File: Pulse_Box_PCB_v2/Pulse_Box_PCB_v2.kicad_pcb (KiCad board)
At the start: 2 copper layers, 80 x 59 mm, 60 parts, among them J1 Screw_Terminal_01x02, J2 Conn_01x11, J3 Conn_01x11, J4 Conn_01x03, J5 Conn_01x03, J6 Conn_01x03_Pin, P1 USB_C_Plug_USB2.0, SW1 SW_Push, SW2 SW_Push, U1 ESP32-S3-WROOM-1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

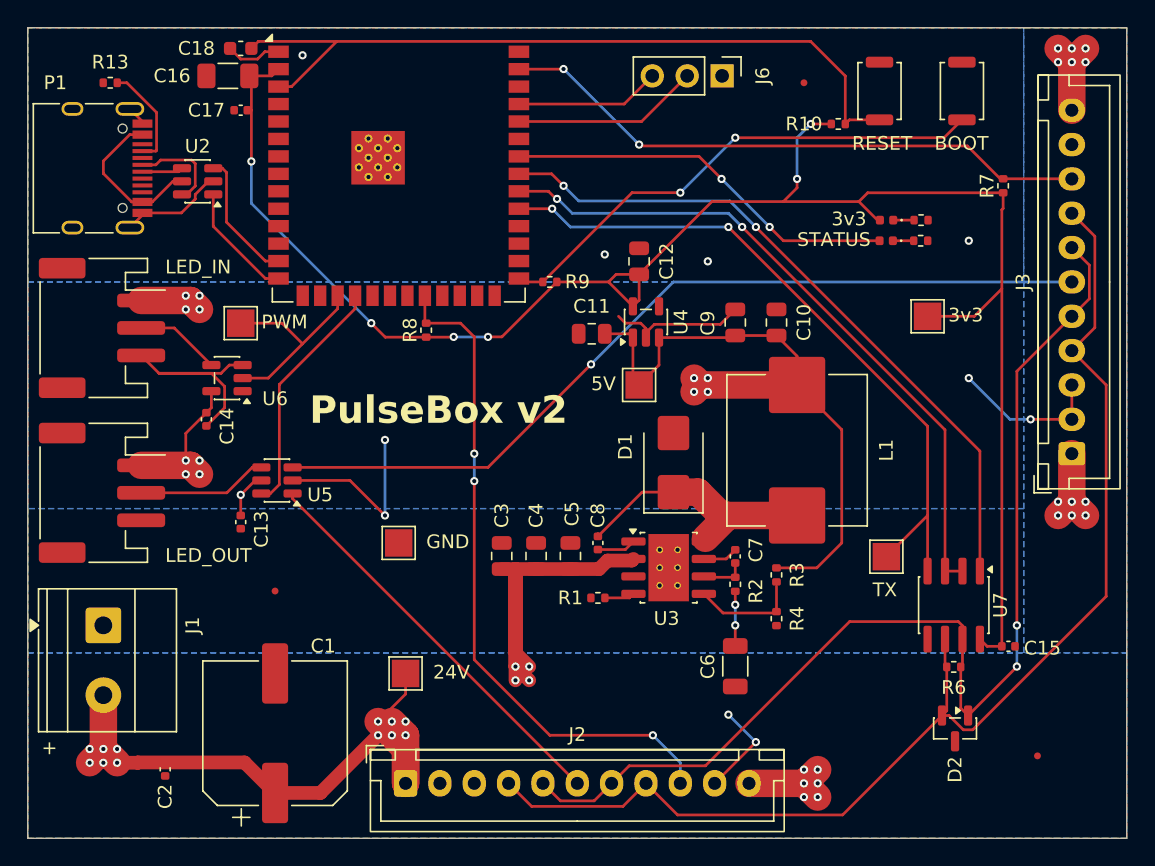
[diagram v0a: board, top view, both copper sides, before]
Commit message: add design for pulsebox panel, update v2 PCB to remove 485 trans
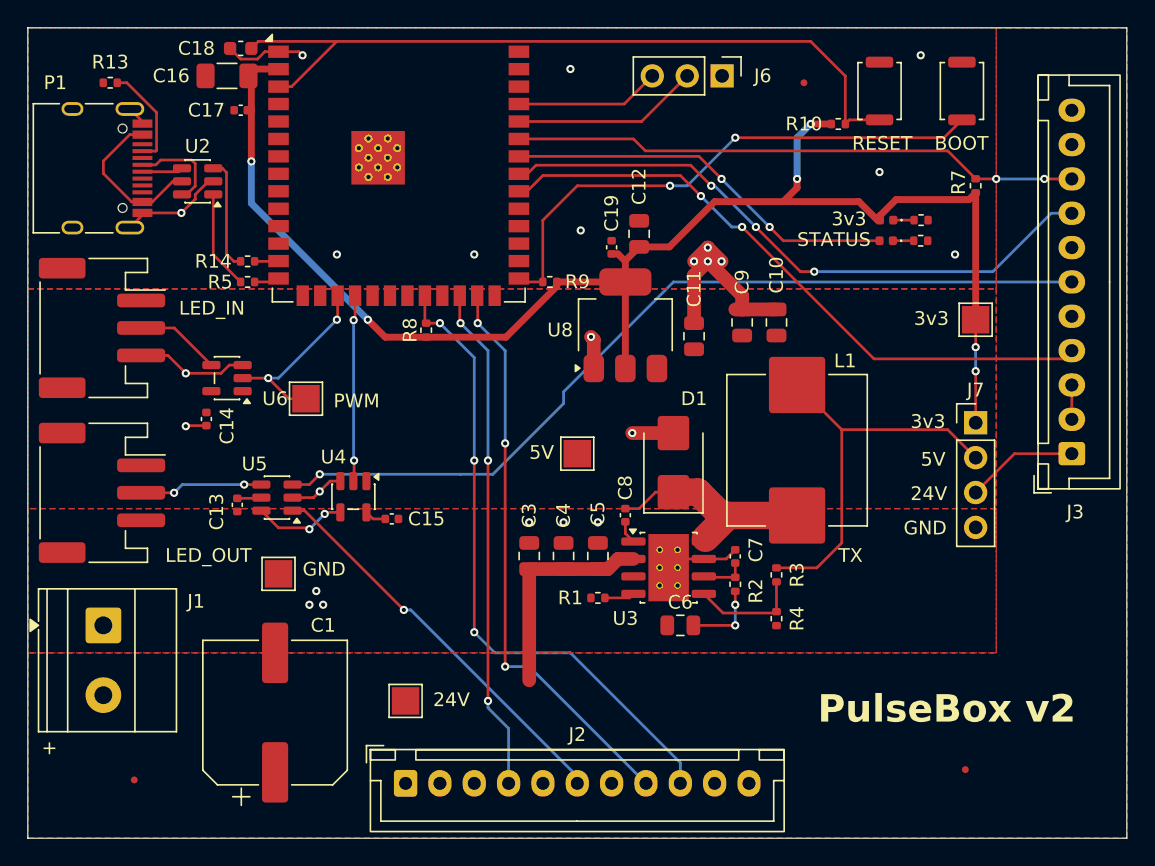
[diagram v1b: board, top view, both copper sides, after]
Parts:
- removed C2: 100nF, Capacitor_SMD:C_0402_1005Metric
- removed D2: SP0502BAHT, Package_TO_SOT_SMD:SOT-23
- removed R6: 120, Resistor_SMD:R_0402_1005Metric
- removed TP6: TestPoint, TestPoint:TestPoint_Pad_2.0x2.0mm
- removed U7: SP3485EN, Package_SO:SOIC-8_3.9x4.9mm_P1.27mm
- added C19: 100nF, Capacitor_SMD:C_0402_1005Metric, F.Cu at (192.5, 67.0)
- added J7: Conn_01x04, Connector_PinHeader_2.54mm:PinHeader_1x04_P2.54mm_Vertical, F.Cu at (219.0, 79.8)
- added R14: 22, Resistor_SMD:R_0402_1005Metric, F.Cu at (166.0, 68.0)
- added R5: 22, Resistor_SMD:R_0402_1005Metric, F.Cu at (166.0, 69.5)
- added U8: AP2114-3.3TRG1, Package_TO_SOT_SMD:SOT-223-3_TabPin2, F.Cu at (193.5, 72.7)
- C11: value 10uF -> 4.7uF
- C6: footprint Capacitor_SMD:C_1206_3216Metric -> Capacitor_SMD:C_0805_2012Metric
- R7, R8: value 47k -> 10k
- U4: value AP2112K-3.3 -> SN74LV1T34DBV
- moved C15 45.8 mm to (176.5, 86.8)
- moved U4 24.8 mm to (173.7, 85.1), turned to -90 degrees
- moved FID1 17.2 mm to (157.8, 105.8)
- moved TP1 9.03 mm to (168.2, 90.8)
- moved C11 7.45 mm to (198.5, 73.5), turned to 90 degrees
- moved TP5 7.27 mm to (170.2, 78.0)
- moved TP3 6.73 mm to (190.0, 82.0)
- moved FID2 5.34 mm to (218.2, 105.0)
- moved C6 4.99 mm to (197.5, 94.5), turned to 0 degrees
- moved TP4 3.51 mm to (219.0, 72.2)
- moved C8 2.84 mm to (193.5, 86.5)
- moved C12 2.00 mm to (194.5, 66.0)
- moved C3 2.00 mm to (186.5, 89.5)
- moved C4 2.00 mm to (189.0, 89.5)
- moved C5 2.00 mm to (191.5, 89.5)
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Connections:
- C15 pad 1: +3.3V -> +5V
- J2 pad 4: 485A -> UART2_TX
- J2 pad 5: 485B -> unconnected-(J2-Pin_5-Pad5)
- J2 pad 7: 485B -> unconnected-(J2-Pin_7-Pad7)
- J2 pad 8: 485A -> UART2_RX
- J3 pad 4: 485A -> UART1_TX
- J3 pad 5: 485B -> unconnected-(J3-Pin_5-Pad5)
- J3 pad 7: 485B -> unconnected-(J3-Pin_7-Pad7)
- J3 pad 8: 485A -> UART1_RX
- U1 pad 24: unconnected-(U1-IO47-Pad24) -> UART2_TX
- U1 pad 25: unconnected-(U1-IO48-Pad25) -> UART2_RX
- U1 pad 31: UART1_TX -> unconnected-(U1-IO38-Pad31)
- U1 pad 32: 485_DE -> UART1_TX
- U1 pad 35: unconnected-(U1-IO42-Pad35) -> E_SENS
- U1 pad 39: E_SENS -> unconnected-(U1-IO1-Pad39)
- U2 pad 1: DP -> Net-(R5-Pad2)
- U2 pad 3: DM -> Net-(R14-Pad2)
- U4 pad 1: +5V -> unconnected-(U4-NC-Pad1)
- U4 pad 2: GND -> PWM_SEL
- U4 pad 3: +5V -> GND
- U4 pad 4: unconnected-(U4-NC-Pad4) -> Net-(U4-Y)
- U4 pad 5: +3.3V -> +5V
- U5 pad 6: PWM_SEL -> Net-(U4-Y)
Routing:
- net 485A: track 89.4 -> 0.00 mm
- net 485B: track 81.7 -> 0.00 mm, vias 2 -> 0
- net +24V: track 96.5 -> 23.7 mm, vias 34 -> 0
- net 485_DE: track 50.1 -> 0.00 mm, vias 2 -> 0
- net UART2_RX: track 0.00 -> 41.6 mm, vias 0 -> 3
- net UART2_TX: track 0.00 -> 37.0 mm, vias 0 -> 3
- net +5V: track 67.9 -> 32.3 mm, vias 13 -> 0
- net +3.3V: track 131.0 -> 107.5 mm
- net GND: track 74.8 -> 58.3 mm, vias 10 -> 24
- net Net-(R14-Pad2): track 0.00 -> 8.27 mm
- net DM: track 9.67 -> 1.75 mm
- net Net-(R5-Pad2): track 0.00 -> 7.20 mm
- net Net-(U4-Y): track 0.00 -> 7.17 mm, vias 0 -> 2
- net DP: track 8.65 -> 1.84 mm
- net UART1_RX: track 50.7 -> 45.5 mm, vias 2 -> 3
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- added copper zone on F.Cu, net +24V
- added copper zone on F.Cu, net +5V
- removed copper zone on B.Cu, net +24V
- removed copper zone on B.Cu, net +5V

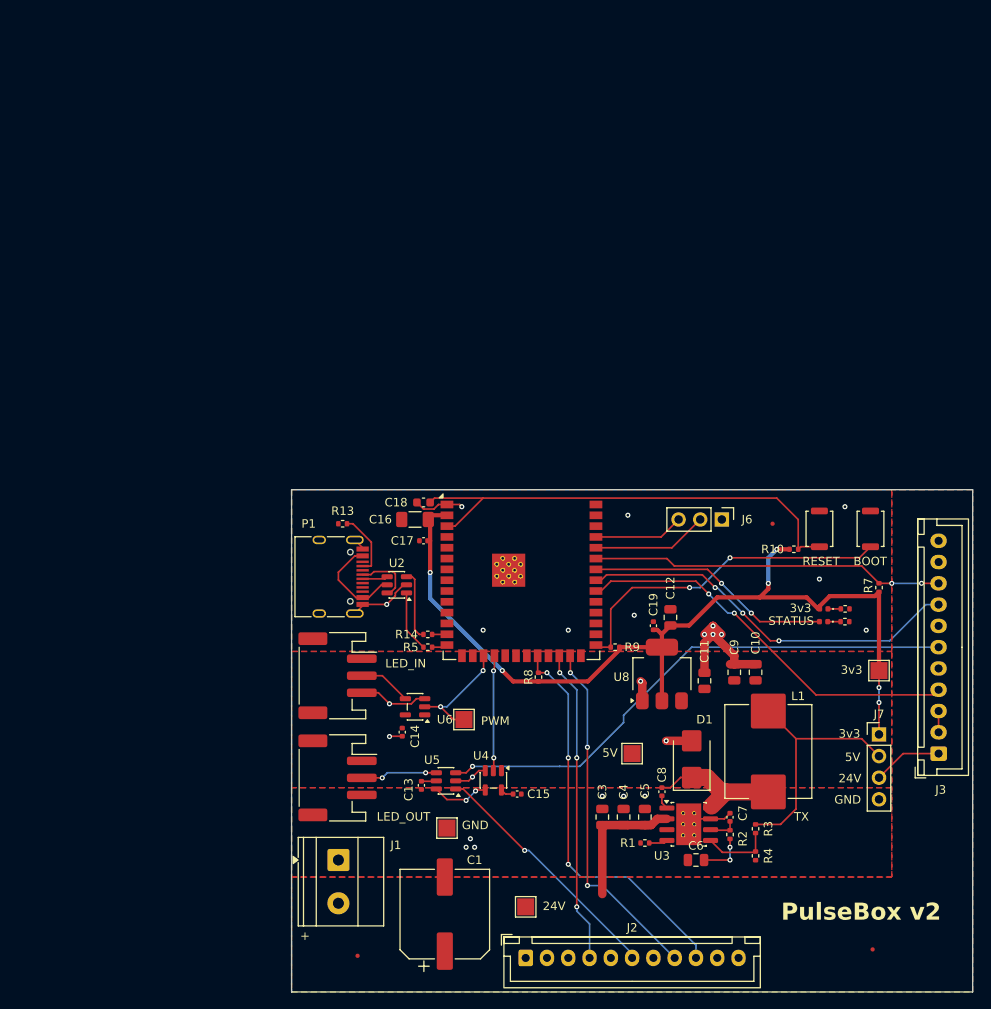
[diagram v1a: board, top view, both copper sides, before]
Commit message: v2 board mirrored layout
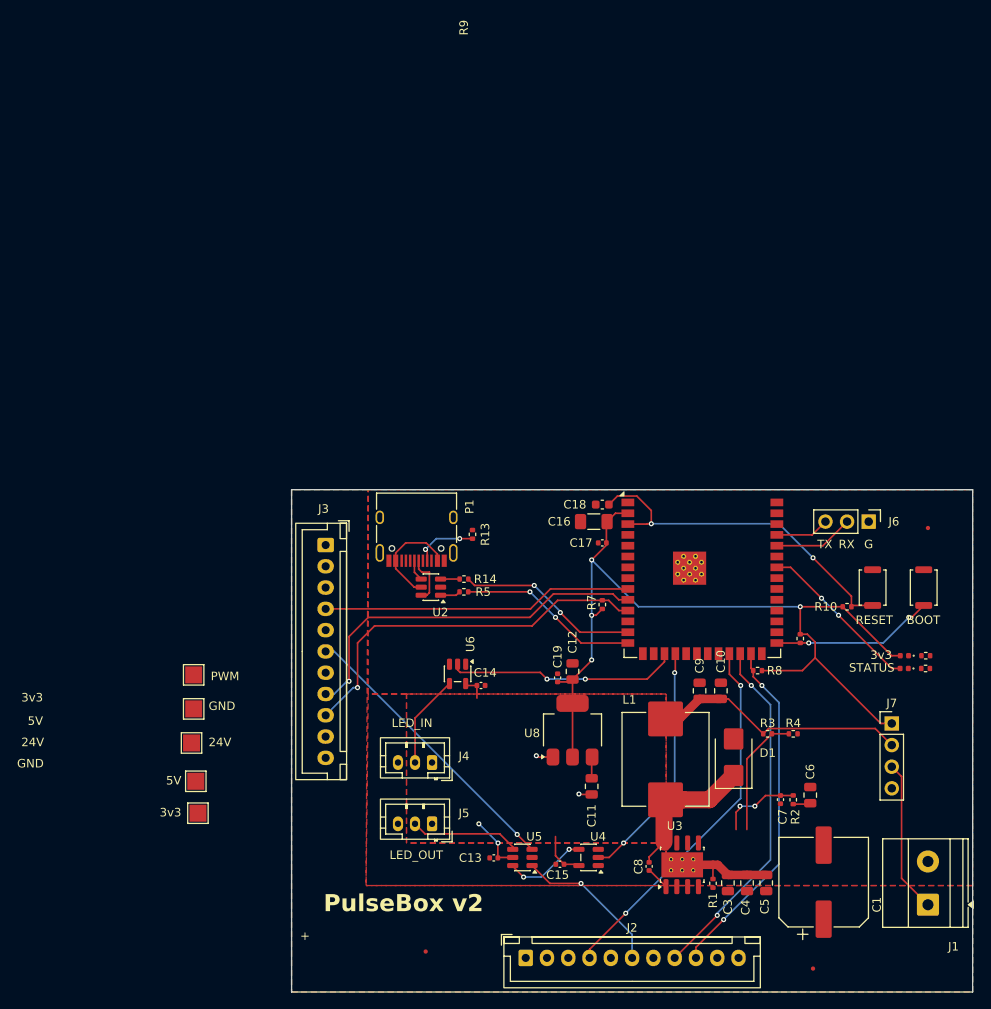
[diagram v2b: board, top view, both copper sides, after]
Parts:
- J4, J5: footprint Connector_JST:JST_PH_S3B-PH-SM4-TB_1x03-1MP_P2.00mm_Horizontal -> Connector_JST:JST_PH_B3B-PH-K_1x03_P2.00mm_Vertical
- moved TP4 81.7 mm to (139.0, 89.0)
- moved J3 76.1 mm to (154.0, 57.5), turned to -90 degrees
- moved J1 69.4 mm to (224.8, 99.8), turned to 90 degrees
- moved TP3 51.4 mm to (138.8, 85.2)
- moved C1 44.7 mm to (212.5, 97.1)
- moved TP2 43.7 mm to (138.2, 80.8)
- moved TP1 32.9 mm to (138.5, 76.8)
- moved R7 32.6 mm to (186.5, 64.5)
- moved TP5 32.2 mm to (138.5, 72.8)
- moved R8 25.8 mm to (204.7, 72.2), turned to 180 degrees
- moved R9 21.8 mm to (209.8, 68.5), turned to -90 degrees
- moved U1 21.3 mm to (198.2, 57.8)
- moved C16 21.0 mm to (185.5, 54.8)
- moved C17 21.0 mm to (186.5, 57.2)
- moved C18 21.0 mm to (186.5, 52.8)
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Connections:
- J1 pad 1: GND -> +24V
- J1 pad 2: +24V -> GND
- J2 pad 9: S_SENS -> N_SENS
- R8 pad 2: S_SENS -> N_SENS
- U1 pad 10: unconnected-(U1-IO17-Pad10) -> UART1_RX
- U1 pad 11: unconnected-(U1-IO18-Pad11) -> E_SENS
- U1 pad 22: S_SENS -> unconnected-(U1-IO14-Pad22)
- U1 pad 23: unconnected-(U1-IO21-Pad23) -> UART2_TX
- U1 pad 24: UART2_TX -> UART2_RX
- U1 pad 25: UART2_RX -> N_SENS
- U1 pad 32: UART1_TX -> unconnected-(U1-IO39-Pad32)
- U1 pad 33: UART1_RX -> unconnected-(U1-IO40-Pad33)
- U1 pad 35: E_SENS -> unconnected-(U1-IO42-Pad35)
- U1 pad 9: unconnected-(U1-IO16-Pad9) -> UART1_TX
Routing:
- net S_SENS: track 47.0 -> 0.00 mm, vias 3 -> 0
- net GND: track 58.3 -> 15.6 mm, vias 24 -> 2
- net N_SENS: track 0.00 -> 41.1 mm, vias 0 -> 2
- net PWM_OUT_E: track 63.3 -> 33.9 mm
- net Net-(U1-IO0): track 39.9 -> 19.1 mm
- net DM: track 1.75 -> 21.4 mm, vias 0 -> 2
- net DP: track 1.84 -> 21.2 mm, vias 0 -> 2
- net +5V: track 32.3 -> 47.8 mm, vias 0 -> 2
- net Net-(U1-EN): track 56.2 -> 41.2 mm, vias 0 -> 2
- net PWM_SEL: track 13.6 -> 28.4 mm
- net PWM_3V3: track 13.8 -> 27.2 mm
- net PWM_OUT_S: track 29.2 -> 17.9 mm
- net UART1_TX: track 46.1 -> 36.5 mm, vias 2 -> 0
- net STATUS: track 28.8 -> 19.4 mm
- net Net-(U3-FB): track 7.58 -> 14.4 mm
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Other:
- board text added: "G"
- board text added: "RX"
